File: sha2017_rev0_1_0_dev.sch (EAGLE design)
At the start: 199 parts, among them IC1 CP210X_USB_UART, IC2 AP7215, IC3 ESP32WROOM32, IC4 MCP73833, IC5 FXL6408, IC6 CPT112, Q2 MMBT2222A, Q3 MMBT2222A, Q4 MMBT2222A, Q5 MMBT2222A, Q6 SI1304 BDL, Q7 MMBT2222A, T1 SI2301DS, T2 SI2301DS, T3 SI2301DS, X1 2908-05WB-MG, X3 JST-PH3

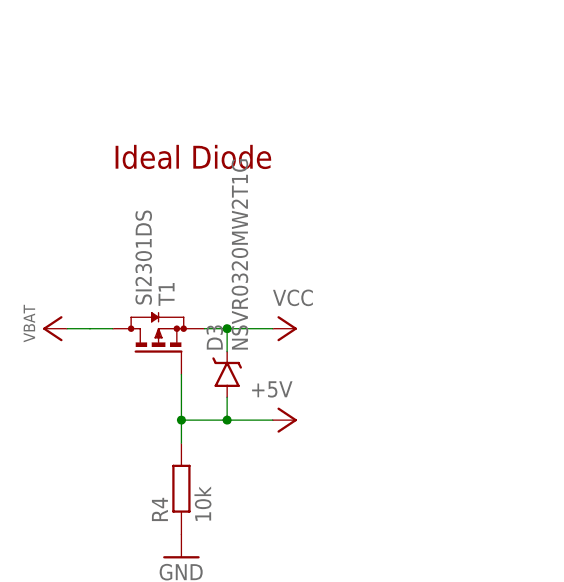
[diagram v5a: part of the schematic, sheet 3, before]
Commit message: fixed bug at powersupply Mosfets was N channel and need to be P channel to switch the Highside voltage
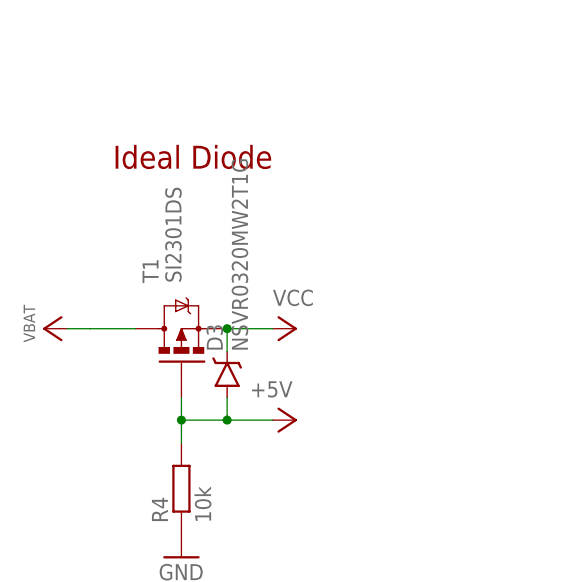
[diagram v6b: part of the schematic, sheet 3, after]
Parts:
- added TP3: TEST-POINT3, SparkFun-Passives:TEST-POINT3
- T1, T2, T3: device transistor-small-signal:BSS84 -> SparkFun-DiscreteSemi:MOSFET-PCHANNEL
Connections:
- net +3V3: now also T3.S
- net 3V3_SWITCHED: now also T3.D
- net GND: now also TP3.1
- net VCC: now also T2.S
- net WS2812_POWER: now also T2.D
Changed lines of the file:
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@@
 <attribute name="PARTNO" value="GRM188R71H104KA93D"/>
 </part>
-<part name="T1" library="transistor-small-signal" deviceset="BSS84" device="" value="SI2301DS"/>
+<part name="T1" library="SparkFun-DiscreteSemi" deviceset="MOSFET-PCHANNEL" device="" value="SI2301DS"/>
 <part name="R4" library="sha2017_rev0_1_0_dev" deviceset="R0603-DASHES" device="" value="10k">
 <attribute name="PARTNO" value="ERJ-3GEYJ103V"/>
@@
 <attribute name="PARTNO" value="GRM21BR61C475KA88K"/>
 </part>
-<part name="T2" library="transistor-small-signal" deviceset="BSS84" device="" value="SI2301DS"/>
-<part name="T3" library="transistor-small-signal" deviceset="BSS84" device="" value="SI2301DS"/>
+<part name="T2" library="SparkFun-DiscreteSemi" deviceset="MOSFET-PCHANNEL" device="" value="SI2301DS"/>
+<part name="T3" library="SparkFun-DiscreteSemi" deviceset="MOSFET-PCHANNEL" device="" value="SI2301DS"/>
+<part name="TP3" library="SparkFun-Passives" deviceset="TEST-POINT" device="3">
+<attribute name="PARTNO" value="NAP"/>
+</part>
+<part name="GND95" library="supply1" deviceset="GND" device=""/>
 </parts>
 <sheets>
@@
 <junction x="139.7" y="101.6"/>
 <pinref part="+3V6" gate="G$1" pin="+3V3"/>
+<pinref part="T3" gate="G$1" pin="S"/>
 </segment>
 <segment>
@@
 <junction x="124.46" y="91.44"/>
 <pinref part="T3" gate="G$1" pin="G"/>
-<wire x1="132.08" y1="91.44" x2="134.62" y2="91.44" width="0.1524" layer="91"/>
+<wire x1="132.08" y1="91.44" x2="132.08" y2="93.98" width="0.1524" layer="91"/>
 </segment>
 </net>
@@
 <pinref part="C38" gate="G$1" pin="1"/>
 <junction x="139.7" y="86.36"/>
+<pinref part="T3" gate="G$1" pin="D"/>
 </segment>
 </net>
@@
 <attribute name="PARTNO" x="116.84" y="194.31" size="5.08" layer="96" display="off"/>
 </instance>
-<instance part="T1" gate="G$1" x="88.9" y="83.82" rot="MR90"/>
+<instance part="T1" gate="G$1" x="91.44" y="83.82" rot="R90"/>
 <instance part="R4" gate="G$1" x="91.44" y="66.04" rot="R90">
 <attribute name="PARTNO" x="91.44" y="66.04" size="5.08" layer="96" display="off"/>
@@
 <wire x1="91.44" y1="73.66" x2="96.52" y2="73.66" width="0.1524" layer="91"/>
 <wire x1="96.52" y1="73.66" x2="101.6" y2="73.66" width="0.1524" layer="91"/>
-<wire x1="91.44" y1="78.74" x2="91.44" y2="73.66" width="0.1524" layer="91"/>
+<wire x1="91.44" y1="76.2" x2="91.44" y2="73.66" width="0.1524" layer="91"/>
 <wire x1="96.52" y1="73.66" x2="96.52" y2="76.2" width="0.1524" layer="91"/>
 <junction x="96.52" y="73.66"/>
@@
 </segment>
 <segment>
-<wire x1="83.82" y1="83.82" x2="81.28" y2="83.82" width="0.1524" layer="91"/>
+<wire x1="86.36" y1="83.82" x2="81.28" y2="83.82" width="0.1524" layer="91"/>
 <wire x1="78.74" y1="83.82" x2="81.28" y2="83.82" width="0.1524" layer="91"/>
 <pinref part="T1" gate="G$1" pin="D"/>
@@
 <net name="VCC" class="1">
 <segment>
-<wire x1="93.98" y1="83.82" x2="96.52" y2="83.82" width="0.1524" layer="91"/>
 <wire x1="96.52" y1="83.82" x2="96.52" y2="81.28" width="0.1524" layer="91"/>
 <wire x1="101.6" y1="83.82" x2="96.52" y2="83.82" width="0.1524" layer="91"/>
@@
 <junction x="66.04" y="86.36"/>
 <pinref part="T2" gate="G$1" pin="G"/>
-<wire x1="73.66" y1="86.36" x2="76.2" y2="86.36" width="0.1524" layer="91"/>
+<wire x1="73.66" y1="86.36" x2="73.66" y2="88.9" width="0.1524" layer="91"/>
 </segment>
 </net>
@@
 <pinref part="C4" gate="G$1" pin="1"/>
 <junction x="81.28" y="81.28"/>
+<pinref part="T2" gate="G$1" pin="D"/>
 </segment>
 </net>
@@
 <junction x="81.28" y="96.52"/>
 <pinref part="P+6" gate="VCC" pin="VCC"/>
+<pinref part="T2" gate="G$1" pin="S"/>
 </segment>
 </net>
@@
 <attribute name="PARTNO" x="63.5" y="160.02" size="5.08" layer="96" display="off"/>
 </instance>
+<instance part="TP3" gate="G$1" x="63.5" y="144.78" rot="R90">
+<attribute name="PARTNO" x="63.5" y="144.78" size="5.08" layer="96" rot="R180" display="off"/>
+</instance>
+<instance part="GND95" gate="1" x="63.5" y="142.24"/>
 </instances>
 <busses>
@@
 <pinref part="GND86" gate="1" pin="GND"/>
 </segment>
+<segment>
+<pinref part="TP3" gate="G$1" pin="1"/>
+<pinref part="GND95" gate="1" pin="GND"/>
+</segment>
 </net>
 <net name="TOUCH_INT" class="0">
@@
 <wire x1="63.5" y1="160.02" x2="55.88" y2="160.02" width="0.1524" layer="91"/>
 <junction x="63.5" y="160.02"/>
+<wire x1="96.52" y1="160.02" x2="63.5" y2="160.02" width="0.1524" layer="91"/>
 </segment>
 </net>

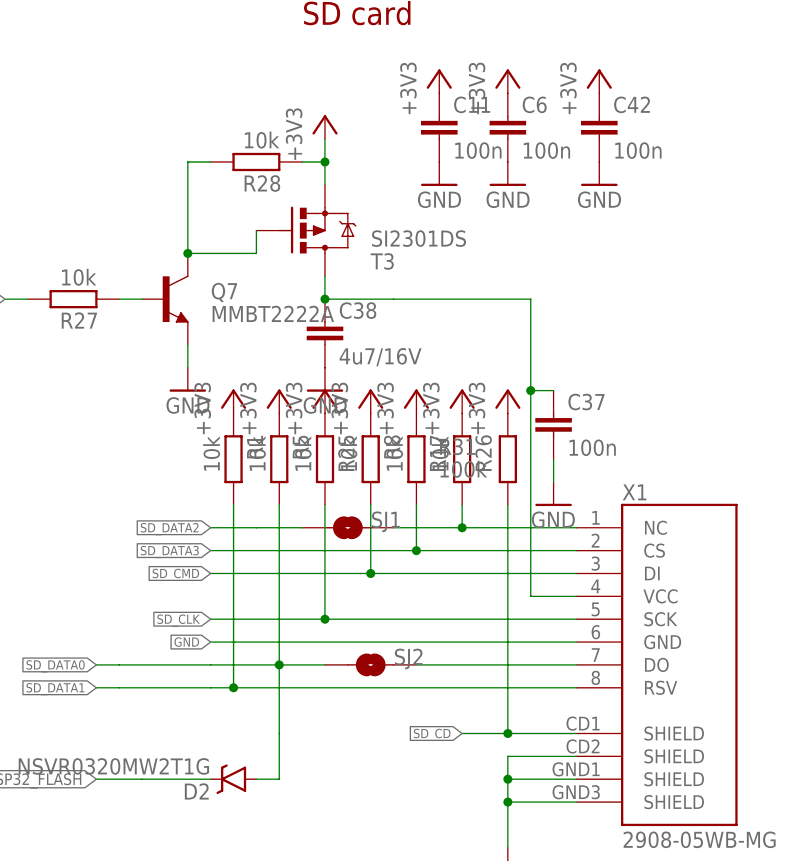
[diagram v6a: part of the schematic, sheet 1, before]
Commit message: fixed pinswap at sd card
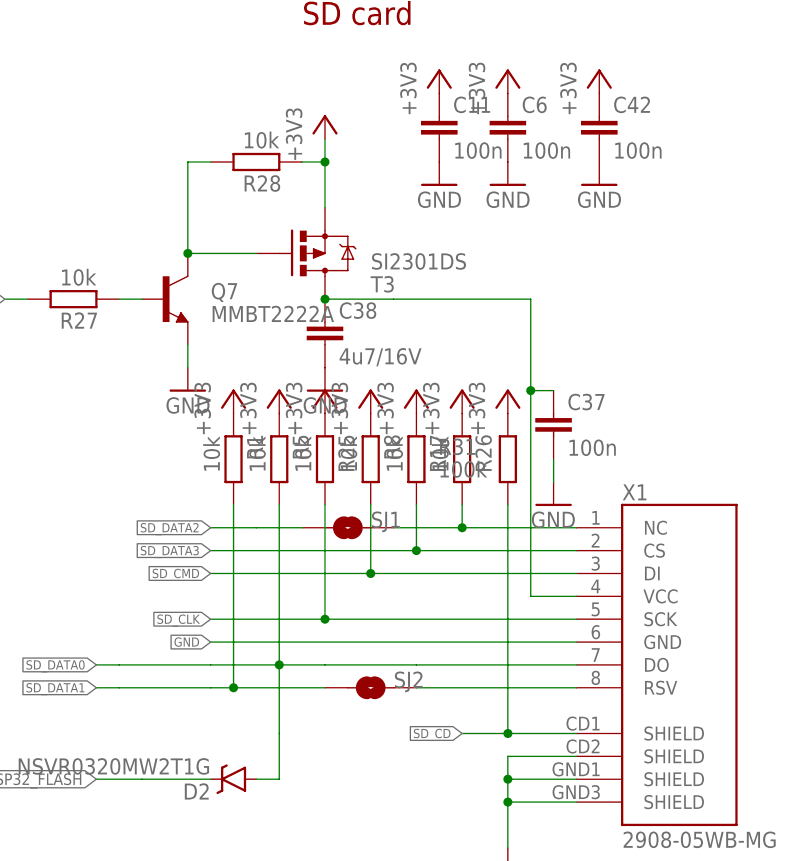
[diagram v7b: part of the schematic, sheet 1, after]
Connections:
- removed net N$20: SJ2.2, X1.DO
- new net N$6: SJ2.2, X1.RSV
- net SD_DATA0: now also X1.DO; no longer SJ2.1
- net SD_DATA1: now also SJ2.1; no longer X1.RSV
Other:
- moved on the sheet: SJ2, T2, T3
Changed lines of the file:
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@@
-<attribute name="PARTNO" value="NAP"/>
-</part>
-<part name="SJ2" library="SparkFun-Passives" deviceset="JUMPER-PAD-2-NO" device="YES_SILK">
 <attribute name="PARTNO" value="NAP"/>
 </part>
@@
 </part>
 <part name="GND95" library="supply1" deviceset="GND" device=""/>
+<part name="SJ2" library="SparkFun-Passives" deviceset="JUMPER-PAD-2-NO" device="YES_SILK">
+<attribute name="PARTNO" value="NAP"/>
+</part>
 </parts>
 <sheets>
@@
 <attribute name="PARTNO" x="142.24" y="60.96" size="1.778" layer="96" display="off"/>
 </instance>
-<instance part="SJ2" gate="G$1" x="144.78" y="45.72" smashed="yes">
-<attribute name="NAME" x="147.32" y="45.72" size="1.778" layer="95"/>
-<attribute name="PARTNO" x="144.78" y="45.72" size="1.778" layer="96" display="off"/>
-</instance>
 <instance part="TP5" gate="G$1" x="43.18" y="172.72">
 <attribute name="PARTNO" x="43.18" y="172.72" size="5.08" layer="96" rot="R270" display="off"/>
@@
 <attribute name="PARTNO" x="139.7" y="83.82" size="1.778" layer="96" rot="MR0" display="off"/>
 </instance>
-<instance part="T3" gate="G$1" x="139.7" y="93.98" rot="MR180"/>
+<instance part="T3" gate="G$1" x="139.7" y="91.44" rot="MR180"/>
+<instance part="SJ2" gate="G$1" x="144.78" y="43.18" smashed="yes">
+<attribute name="NAME" x="147.32" y="43.18" size="1.778" layer="95"/>
+<attribute name="PARTNO" x="144.78" y="43.18" size="1.778" layer="96" display="off"/>
+</instance>
 </instances>
 <busses>
@@
 <wire x1="137.16" y1="101.6" x2="139.7" y2="101.6" width="0.1524" layer="91"/>
 <wire x1="139.7" y1="101.6" x2="139.7" y2="104.14" width="0.1524" layer="91"/>
-<wire x1="139.7" y1="101.6" x2="139.7" y2="99.06" width="0.1524" layer="91"/>
+<wire x1="139.7" y1="101.6" x2="139.7" y2="96.52" width="0.1524" layer="91"/>
 <junction x="139.7" y="101.6"/>
 <pinref part="+3V6" gate="G$1" pin="+3V3"/>
@@
 <wire x1="134.62" y1="33.02" x2="134.62" y2="38.1" width="0.1524" layer="91"/>
 <wire x1="116.84" y1="45.72" x2="127" y2="45.72" width="0.1524" layer="91"/>
-<pinref part="SJ2" gate="G$1" pin="1"/>
+<pinref part="X1" gate="G$1" pin="DO"/>
+<wire x1="167.64" y1="45.72" x2="149.86" y2="45.72" width="0.1524" layer="91"/>
+<wire x1="139.7" y1="45.72" x2="149.86" y2="45.72" width="0.1524" layer="91"/>
 </segment>
 </net>
@@
 <wire x1="116.84" y1="43.18" x2="114.3" y2="43.18" width="0.1524" layer="91"/>
 <label x="114.3" y="43.18" size="1.016" layer="95" rot="R180" xref="yes"/>
-<pinref part="X1" gate="G$1" pin="RSV"/>
-<wire x1="167.64" y1="43.18" x2="129.54" y2="43.18" width="0.1524" layer="91"/>
 <pinref part="R1" gate="G$1" pin="1"/>
+<wire x1="139.7" y1="43.18" x2="129.54" y2="43.18" width="0.1524" layer="91"/>
 <wire x1="129.54" y1="43.18" x2="127" y2="43.18" width="0.1524" layer="91"/>
 <wire x1="129.54" y1="63.5" x2="129.54" y2="43.18" width="0.1524" layer="91"/>
 <junction x="129.54" y="43.18"/>
 <wire x1="116.84" y1="43.18" x2="127" y2="43.18" width="0.1524" layer="91"/>
+<pinref part="SJ2" gate="G$1" pin="1"/>
 </segment>
 </net>
@@
 <junction x="124.46" y="91.44"/>
 <pinref part="T3" gate="G$1" pin="G"/>
-<wire x1="132.08" y1="91.44" x2="132.08" y2="93.98" width="0.1524" layer="91"/>
 </segment>
 </net>
 <net name="3V3_SWITCHED" class="0">
 <segment>
-<wire x1="139.7" y1="86.36" x2="139.7" y2="88.9" width="0.1524" layer="91"/>
 <wire x1="139.7" y1="86.36" x2="147.32" y2="86.36" width="0.1524" layer="91"/>
 <pinref part="X1" gate="G$1" pin="VCC"/>
@@
 </segment>
 </net>
-<net name="N$20" class="0">
-<segment>
-<pinref part="X1" gate="G$1" pin="DO"/>
-<wire x1="167.64" y1="45.72" x2="149.86" y2="45.72" width="0.1524" layer="91"/>
-<pinref part="SJ2" gate="G$1" pin="2"/>
-</segment>
-</net>
 <net name="SD_DATA2_OUT" class="0">
 <segment>
@@
 <wire x1="132.08" y1="60.96" x2="127" y2="60.96" width="0.1524" layer="91"/>
 <label x="127" y="60.96" size="1.016" layer="95" rot="R180" xref="yes"/>
+</segment>
+</net>
+<net name="N$6" class="0">
+<segment>
+<pinref part="X1" gate="G$1" pin="RSV"/>
+<wire x1="167.64" y1="43.18" x2="149.86" y2="43.18" width="0.1524" layer="91"/>
+<pinref part="SJ2" gate="G$1" pin="2"/>
 </segment>
 </net>
@@
 <attribute name="PARTNO" x="81.28" y="78.74" size="1.778" layer="96" rot="MR0" display="off"/>
 </instance>
-<instance part="T2" gate="G$1" x="81.28" y="88.9" rot="MR180"/>
+<instance part="T2" gate="G$1" x="81.28" y="86.36" rot="MR180"/>
 </instances>
 <busses>
@@
 <junction x="66.04" y="86.36"/>
 <pinref part="T2" gate="G$1" pin="G"/>
-<wire x1="73.66" y1="86.36" x2="73.66" y2="88.9" width="0.1524" layer="91"/>
 </segment>
 </net>
@@
 <net name="WS2812_POWER" class="0">
 <segment>
-<wire x1="81.28" y1="81.28" x2="81.28" y2="83.82" width="0.1524" layer="91"/>
 <wire x1="81.28" y1="81.28" x2="88.9" y2="81.28" width="0.1524" layer="91"/>
 <wire x1="88.9" y1="81.28" x2="88.9" y2="101.6" width="0.1524" layer="91"/>
@@
 <wire x1="78.74" y1="96.52" x2="81.28" y2="96.52" width="0.1524" layer="91"/>
 <wire x1="81.28" y1="96.52" x2="81.28" y2="99.06" width="0.1524" layer="91"/>
-<wire x1="81.28" y1="96.52" x2="81.28" y2="93.98" width="0.1524" layer="91"/>
+<wire x1="81.28" y1="96.52" x2="81.28" y2="91.44" width="0.1524" layer="91"/>
 <junction x="81.28" y="96.52"/>
 <pinref part="P+6" gate="VCC" pin="VCC"/>

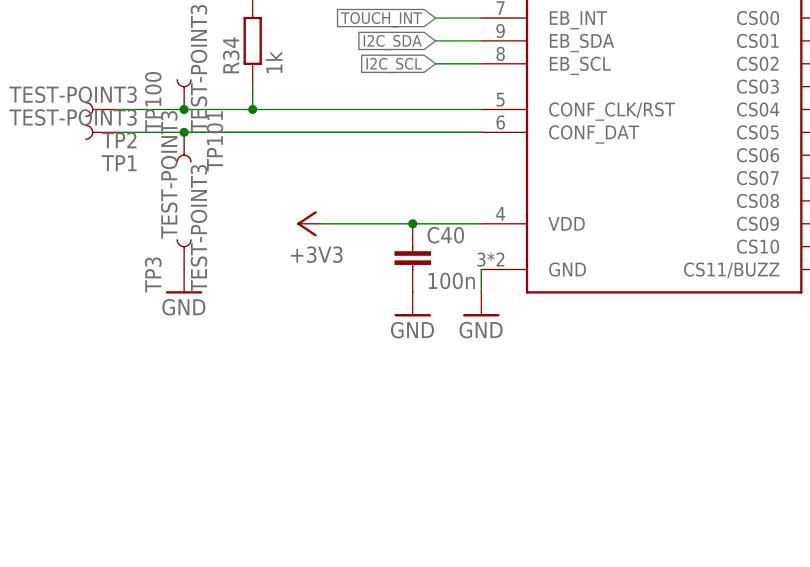
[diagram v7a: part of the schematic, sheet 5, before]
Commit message: added 4,7µF decopling capacitor to the cpt112s power rails
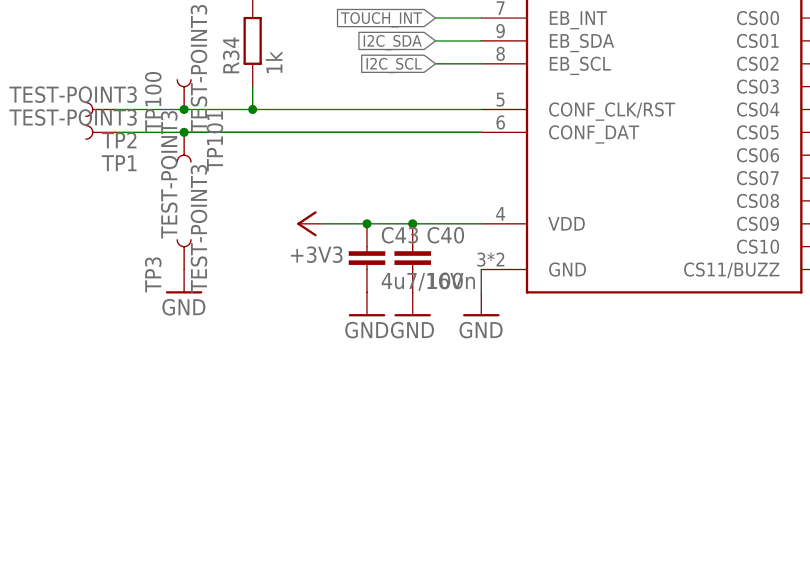
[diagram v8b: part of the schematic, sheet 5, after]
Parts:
- added C43: 4u7/16V, rcl:C-EUC0805
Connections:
- net +3V3: now also C43.1
- net GND: now also C43.2
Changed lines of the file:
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@@
 <attribute name="PARTNO" value="NAP"/>
 </part>
+<part name="C43" library="rcl" deviceset="C-EU" device="C0805" value="4u7/16V">
+<attribute name="PARTNO" value="GRM21BR61C475KA88K"/>
+</part>
+<part name="GND96" library="supply1" deviceset="GND" device=""/>
 </parts>
 <sheets>
@@
 </instance>
 <instance part="GND95" gate="1" x="63.5" y="142.24"/>
+<instance part="C43" gate="G$1" x="83.82" y="147.32">
+<attribute name="PARTNO" x="83.82" y="147.32" size="1.778" layer="96" rot="MR0" display="off"/>
+</instance>
+<instance part="GND96" gate="1" x="83.82" y="139.7"/>
 </instances>
 <busses>
@@
 <pinref part="+3V4" gate="G$1" pin="+3V3"/>
 <pinref part="C40" gate="G$1" pin="1"/>
-<wire x1="78.74" y1="149.86" x2="88.9" y2="149.86" width="0.1524" layer="91"/>
+<wire x1="78.74" y1="149.86" x2="83.82" y2="149.86" width="0.1524" layer="91"/>
 <pinref part="IC6" gate="G$1" pin="VDD"/>
+<wire x1="83.82" y1="149.86" x2="88.9" y2="149.86" width="0.1524" layer="91"/>
 <wire x1="96.52" y1="149.86" x2="88.9" y2="149.86" width="0.1524" layer="91"/>
 <junction x="88.9" y="149.86"/>
+<pinref part="C43" gate="G$1" pin="1"/>
+<junction x="83.82" y="149.86"/>
 </segment>
 <segment>
@@
 <pinref part="GND95" gate="1" pin="GND"/>
 </segment>
+<segment>
+<pinref part="C43" gate="G$1" pin="2"/>
+<pinref part="GND96" gate="1" pin="GND"/>
+</segment>
 </net>
